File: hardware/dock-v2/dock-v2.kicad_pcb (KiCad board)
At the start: 4 copper layers, 100 x 100 mm, 148 parts, among them J101 TYPE-C-31-M-12, J201 TYPE-C-31-M-12, J202 TYPE-C-31-M-12, J203 TYPE-C-31-M-12, J601 Pogo 7-pin, Q601 2N7002, Q602 2N7002, SW301 SW_Push, SW302 SW_Push, SW401 SW_Push, U101 TPD4E1U06DBVR, U102 CH224A, U103 TPS54331DR, U104 AMS1117-3.3, U201 TPD4E1U06DBVR, U202 SY6280AAC, U203 TPD4E1U06DBVR, U204 TPD4E1U06DBVR, U301 RP2354A, U401 RP2354A, U501 ESP32-C3-MINI-1-H4X, U601 TPD4E1U06DBVR, U602 SY6280AAC, Y301 12MHz, Y401 12MHz

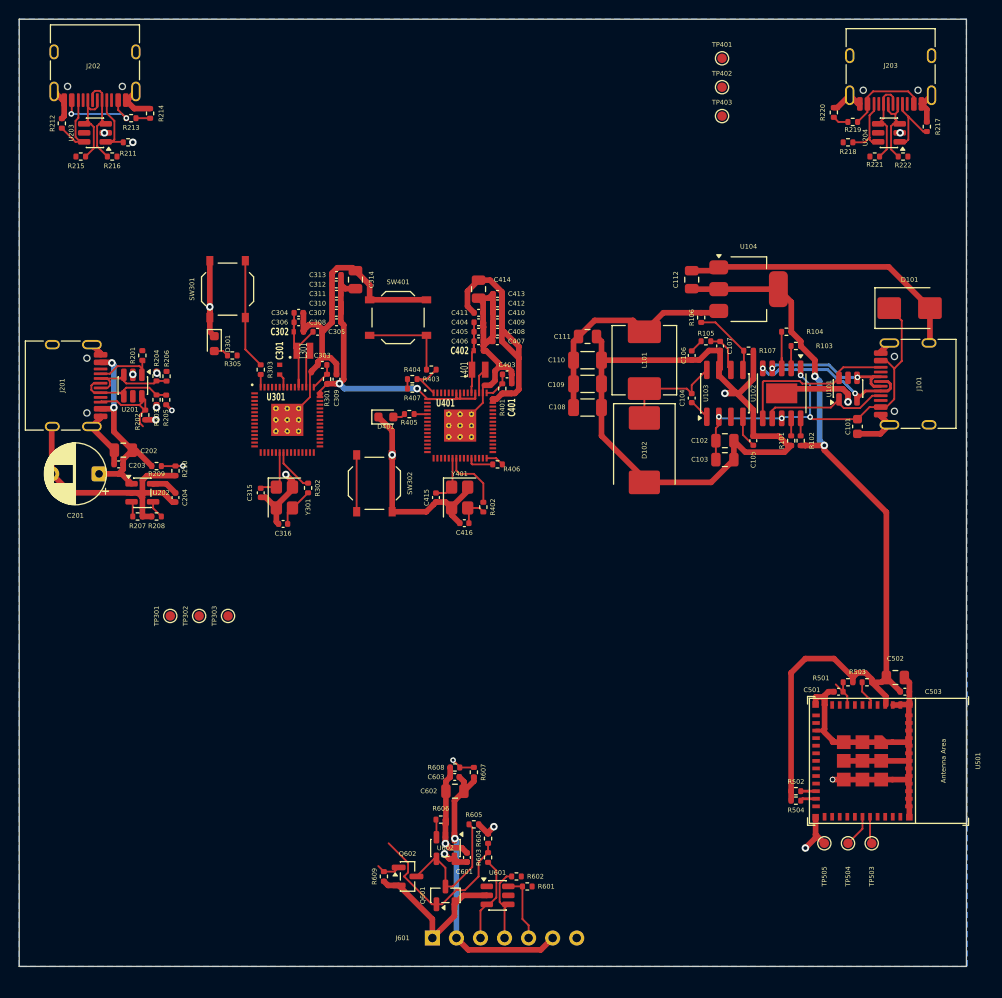
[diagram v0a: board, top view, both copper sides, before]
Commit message: Dock v2: routing complete, SWD test pads removed (user's work, snapshot)
Co-Authored-By: Claude Opus 5.5 <noreply@anthropic.com>
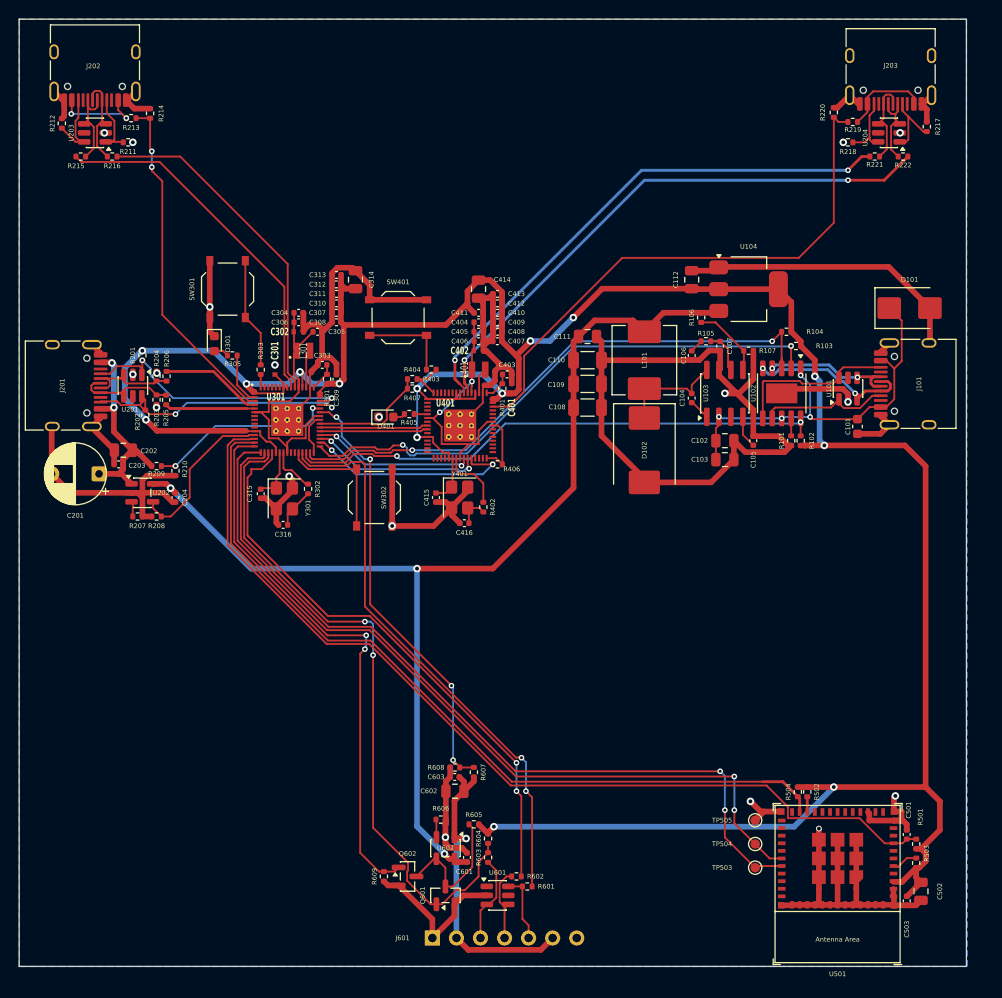
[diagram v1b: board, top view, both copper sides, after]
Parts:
- removed TP301, TP302, TP303, TP401, TP402, TP403: TestPoint, TestPoint:TestPoint_Pad_D1.0mm
- moved C502 22.7 mm to (224.2, 127.1), turned to 90 degrees
- moved C503 22.1 mm to (222.7, 128.1), turned to 90 degrees
- moved R503 19.8 mm to (223.7, 124.1), turned to -90 degrees
- moved R501 18.5 mm to (223.7, 122.1), turned to -90 degrees
- moved C501 16.7 mm to (222.7, 121.1), turned to -90 degrees
- moved U501 14.0 mm to (215.4, 126.3), turned to 180 degrees
- moved TP503 12.6 mm to (206.7, 124.6), turned to -90 degrees
- moved TP504 9.80 mm to (206.7, 122.1), turned to -90 degrees
- moved TP505 7.69 mm to (206.7, 119.6), turned to -90 degrees
- moved SW302 1.50 mm to (166.5, 85.5)
- moved R502 1.20 mm to (212.2, 116.6), turned to -90 degrees
- moved R504 0.95 mm to (211.2, 116.6), turned to -90 degrees
- moved C301 0.50 mm to (156.0, 72.0)
- moved C316 0.10 mm to (156.9, 88.4)
- moved R302 0.10 mm to (159.5, 84.6)
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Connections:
- R305 pad 1: Net-(U301-GPIO2) -> Net-(U301-GPIO0)
- U301 pad 10: KBD_USB_DN -> unconnected-(U301-GPIO7-Pad10)
- U301 pad 12: BLE_TX -> KBD_VBUS_EN
- U301 pad 13: BLE_RX -> BLE_EN
- U301 pad 14: BLE_EN -> BLE_BOOT
- U301 pad 15: BLE_BOOT -> POGO_OFF
- U301 pad 16: POGO_TX -> BLE_TX
- U301 pad 17: POGO_RX -> BLE_RX
- U301 pad 19: POGO_OFF -> POGO_RX
- U301 pad 2: PRS_VBUS_DET -> Net-(U301-GPIO0)
- U301 pad 24: Net-(U301-SWCLK) -> unconnected-(U301-SWCLK-Pad24)
- U301 pad 25: Net-(U301-SWDIO) -> unconnected-(U301-SWDIO-Pad25)
- U301 pad 27: B_LINK_TX -> POGO_TX
- U301 pad 28: B_LINK_RX -> PD_PG
- U301 pad 29: B_RUN -> PD_SDA
- U301 pad 3: unconnected-(U301-GPIO1-Pad3) -> PRS_VBUS_DET
- U301 pad 31: B_BOOTSEL -> PD_SCL
- U301 pad 32: PD_SDA -> B_RUN
- U301 pad 33: PD_SCL -> B_SWDIO
- U301 pad 34: PD_PG -> B_SWCLK
- U301 pad 35: B_SWCLK -> B_LINK_RX
- U301 pad 36: B_SWDIO -> B_LINK_TX
- U301 pad 37: unconnected-(U301-GPIO25-Pad37) -> B_BOOTSEL
- U301 pad 4: Net-(U301-GPIO2) -> KBD_USB_DN
- U301 pad 40: KBD_CC1 -> POGO_5V_SENSE
- U301 pad 41: KBD_CC2 -> KBD_VBUS_SENSE
- U301 pad 42: KBD_VBUS_SENSE -> KBD_CC2
- U301 pad 43: POGO_5V_SENSE -> KBD_CC1
- U301 pad 5: unconnected-(U301-GPIO3-Pad5) -> KBD_USB_DP
- U301 pad 8: KBD_VBUS_EN -> unconnected-(U301-GPIO5-Pad8)
- U301 pad 9: KBD_USB_DP -> unconnected-(U301-GPIO6-Pad9)
- U401 pad 2: B_LINK_RX -> unconnected-(U401-GPIO0-Pad2)
- U401 pad 3: B_LINK_TX -> unconnected-(U401-GPIO1-Pad3)
- U401 pad 4: WRK_VBUS_DET -> unconnected-(U401-GPIO2-Pad4)
- U401 pad 43: unconnected-(U401-GPIO29/ADC3-Pad43) -> WRK_VBUS_DET
- U401 pad 8: unconnected-(U401-GPIO5-Pad8) -> B_LINK_TX
- U401 pad 9: unconnected-(U401-GPIO6-Pad9) -> B_LINK_RX
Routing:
- net 3V3_PWR: track 161.4 -> 324.6 mm, vias 6 -> 14
- net BLE_EN: track 3.69 -> 100.3 mm
- net 5V_PWR: track 30.1 -> 119.5 mm, vias 1 -> 3
- net BLE_BOOT: track 1.70 -> 85.5 mm
- net BLE_RX: track 2.87 -> 86.5 mm, vias 0 -> 2
- net BLE_TX: track 3.43 -> 85.6 mm, vias 0 -> 2
- net POGO_RX: track 0.00 -> 61.0 mm, vias 0 -> 2
- net POGO_TX: track 0.00 -> 60.0 mm, vias 0 -> 2
- net WRK_USB_DN: track 0.00 -> 59.3 mm, vias 0 -> 2
- net WRK_VBUS_DET: track 1.90 -> 59.3 mm
- net WRK_USB_DP: track 0.00 -> 56.8 mm, vias 0 -> 2
- net PD_SCL: track 2.37 -> 58.7 mm, vias 0 -> 2
- net PD_SDA: track 4.96 -> 61.1 mm, vias 0 -> 2
- net POGO_OFF: track 2.58 -> 58.3 mm, vias 0 -> 2
- net PD_PG: track 1.93 -> 57.1 mm, vias 0 -> 2
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
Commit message: Dock v2 PCB: fix unconnected nets, widen power traces, readable silkscreen, 2 copper layers
- MCU A and B IOVDD (pins 30/38) had no 3V3 feed: added an under-chip jumper (A)
  and a top-layer feed to the 3V3 via by the buck (B)
- MCU B's exposed pad sat in a GND pour island: 3V3 bottom ring via moved so the
  plane reaches it; crystal B GND vias added; pour clearance 0.5 -> 0.3 mm
- power traces widened where clearance allows (switch node 1.5 mm, 5 V 1.0 mm,
  VBUS_IN/POGO_5V/KBD_VBUS as far as fits); VBUS_IN vias 0.8/0.4
- silkscreen: refs 0.8/1.0 mm, re-placed clear of pads and parts, labels for
  connectors, buttons, LEDs and ESP32 UART pads; 22 small passives hidden
- copper layers 4 -> 2 (inner layers were empty)
- model/docs: SWD test pads TP301-303/TP401-403 removed

DRC: 0 violations, 0 unconnected, 0 parity issues.

Co-Authored-By: Claude Opus 5.5 <noreply@anthropic.com>
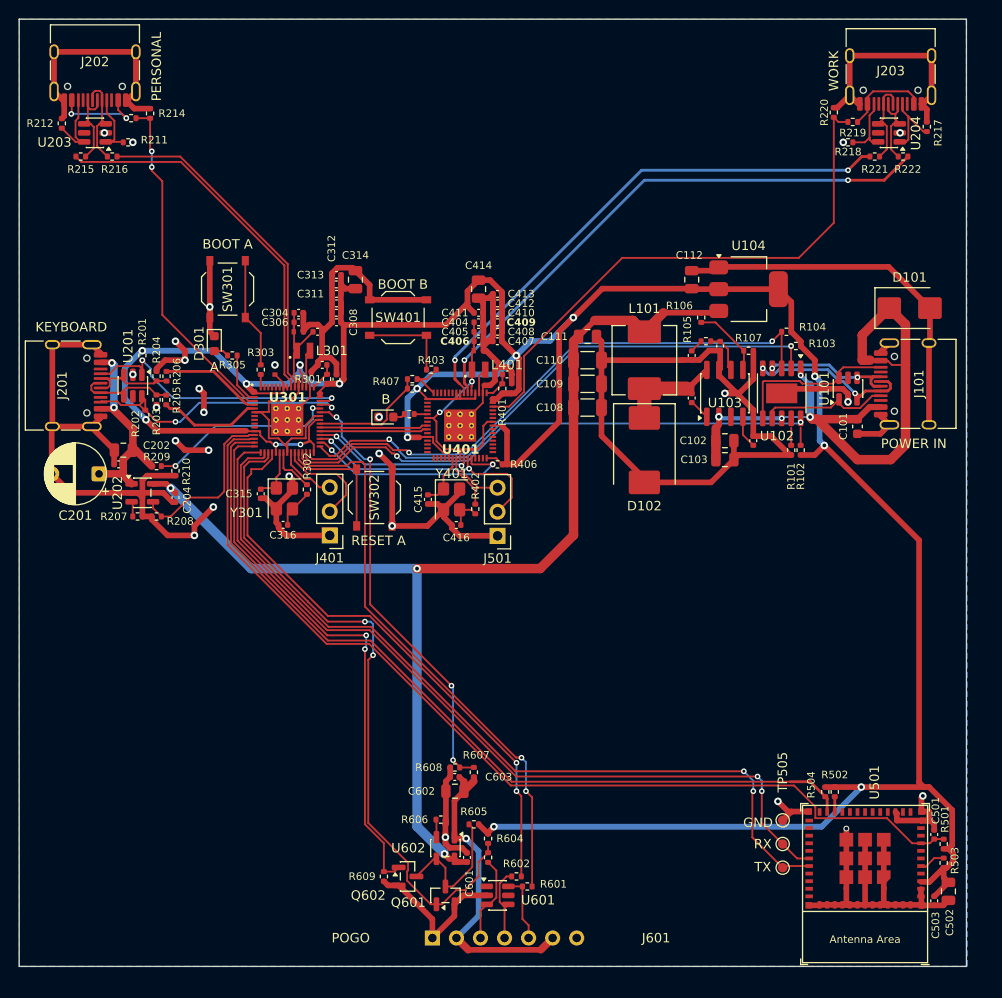
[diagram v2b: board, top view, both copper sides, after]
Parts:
- added J401: Conn_01x03, Connector_PinHeader_2.54mm:PinHeader_1x03_P2.54mm_Vertical, F.Cu at (161.8, 89.5)
- added J501: Conn_01x03, Connector_PinHeader_2.54mm:PinHeader_1x03_P2.54mm_Vertical, F.Cu at (179.5, 89.5)
- moved C501 2.90 mm to (225.6, 121.1)
- moved C502 2.90 mm to (227.1, 127.1)
- moved C503 2.90 mm to (225.6, 128.1)
- moved R501 2.90 mm to (226.6, 122.1)
- moved R502 2.90 mm to (215.1, 116.6)
- moved R503 2.90 mm to (226.6, 124.1)
- moved R504 2.90 mm to (214.1, 116.6)
- moved TP503 2.90 mm to (209.6, 124.6)
- moved TP504 2.90 mm to (209.6, 122.1)
- moved TP505 2.90 mm to (209.6, 119.6)
- moved U501 2.90 mm to (218.3, 126.3)
- moved R101 1.00 mm to (210.5, 80.5)
- moved R102 1.00 mm to (211.5, 80.5)
- moved C415 0.87 mm to (172.2, 85.7)
- moved C416 0.87 mm to (175.1, 88.4)
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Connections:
- R302 pad 1: Net-(C316-Pad2) -> Net-(U301-XOUT)
- R302 pad 2: Net-(U301-XOUT) -> Net-(C316-Pad2)
- U301 pad 24: unconnected-(U301-SWCLK-Pad24) -> Net-(J401-Pin_3)
- U301 pad 25: unconnected-(U301-SWDIO-Pad25) -> Net-(J401-Pin_2)
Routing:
- net GND: track 358.0 -> 452.1 mm, vias 18 -> 26
- net /POWER/VBUS_IN: track 42.1 -> 67.8 mm
- net 3V3_PWR: track 324.6 -> 348.1 mm, vias 14 -> 15
- net Net-(J401-Pin_2): track 0.00 -> 10.9 mm
- net B_SWDIO: track 18.5 -> 27.5 mm
- net Net-(J401-Pin_3): track 0.00 -> 6.36 mm
- net B_SWCLK: track 17.2 -> 22.3 mm
- net 5V_PWR: track 119.5 -> 122.4 mm
- net BLE_EN: track 100.3 -> 103.2 mm
- net BLE_BOOT: track 85.5 -> 88.4 mm
- net BLE_RX: track 86.5 -> 89.2 mm
- net BLE_TX: track 85.6 -> 88.2 mm
- net /MCU_B/B_1V1: track 28.7 -> 30.3 mm
- net KBD_USB_DP: track 9.50 -> 10.9 mm
- net PRS_USB_DP: track 38.6 -> 39.9 mm
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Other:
- copper layers 4 -> 2
- board text added: "A"
- board text added: "B"
- board text added: "BOOT A"
- board text added: "BOOT B"
- board text added: "GND"
- board text added: "KEYBOARD"
- board text added: "PERSONAL"
- board text added: "POGO"
- board text added: "POWER IN"
- board text added: "RESET A"
- board text added: "RX"
- board text added: "TX"
- board text added: "WORK"

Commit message: Dock v2: six M3 mounting holes, U102 CFG1/PG tracks joined, SWD headers in the model
- H1-H6 (MountingHole_3.2mm_M3, unplated) added to the root schematic and placed:
  back (146,39)/(212,39) beside the USB-C ports, sides (133,58)/(225,58),
  front (160,131)/(200,131) either side of the pogo; symmetric about x = 179-180,
  clear of the ESP32 antenna
- R101/R102 tracks ended 1 mm short of U102 pins 9/10: joined
- J401 (SWD A) and J501 (SWD B) added to the connection model and docs

DRC: 0 violations, 0 unconnected, 0 parity issues. ERC: 1 old warning.

Co-Authored-By: Claude Opus 5.5 <noreply@anthropic.com>
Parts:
- added H1: M3, MountingHole:MountingHole_3.2mm_M3, F.Cu at (146.0, 39.0)
- added H2: M3, MountingHole:MountingHole_3.2mm_M3, F.Cu at (212.0, 39.0)
- added H3: M3, MountingHole:MountingHole_3.2mm_M3, F.Cu at (133.0, 58.0)
- added H4: M3, MountingHole:MountingHole_3.2mm_M3, F.Cu at (225.0, 58.0)
- added H5: M3, MountingHole:MountingHole_3.2mm_M3, F.Cu at (160.0, 131.0)
- added H6: M3, MountingHole:MountingHole_3.2mm_M3, F.Cu at (200.0, 131.0)
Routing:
- net Net-(U102-CFG1): track 1.85 -> 2.85 mm
- net PD_PG: track 57.8 -> 58.4 mm

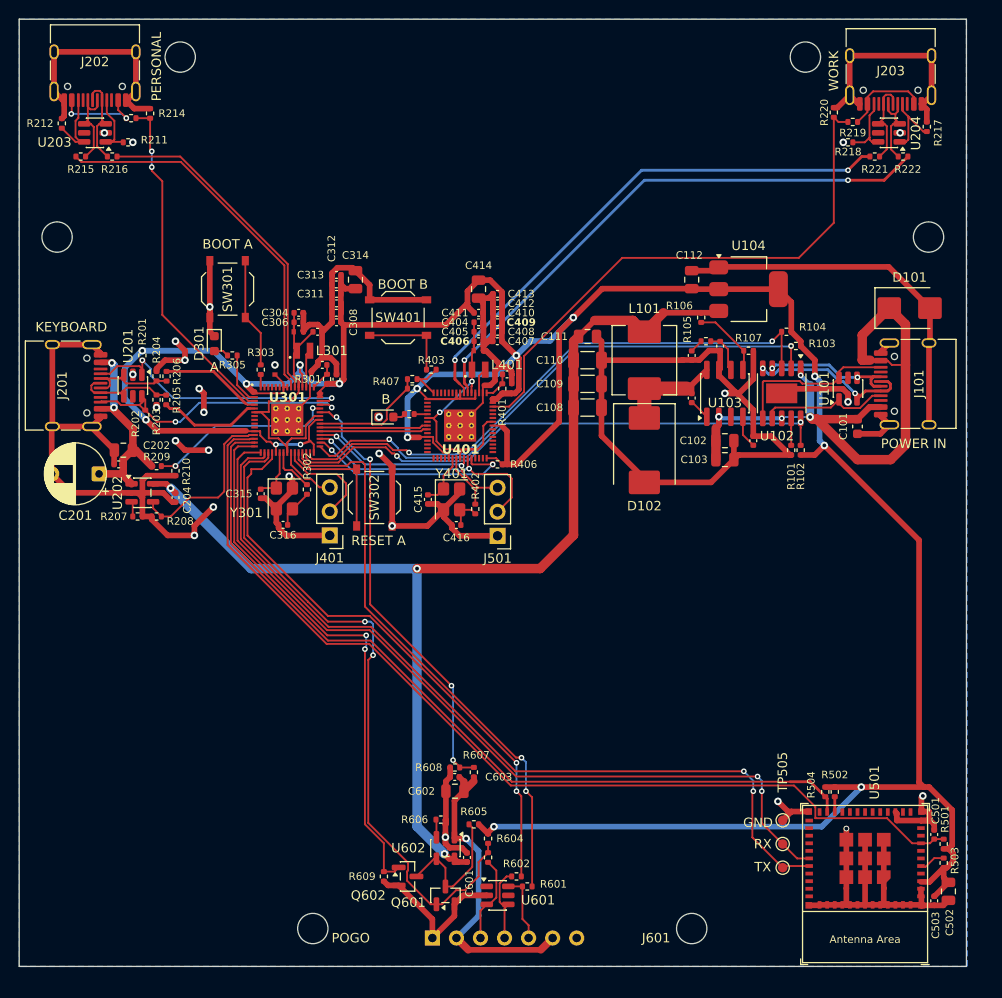
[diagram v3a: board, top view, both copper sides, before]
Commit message: Dock v2: extra mounting holes around the USB-C ports (user's work), H7-H10 given own symbols
The four added holes were copies of H5 (same reference and schematic link);
renamed H7-H10 with their own MountingHole symbols on the root sheet.
DRC: 0 violations, 0 unconnected, 0 parity issues.

Co-Authored-By: Claude Opus 5.5 <noreply@anthropic.com>
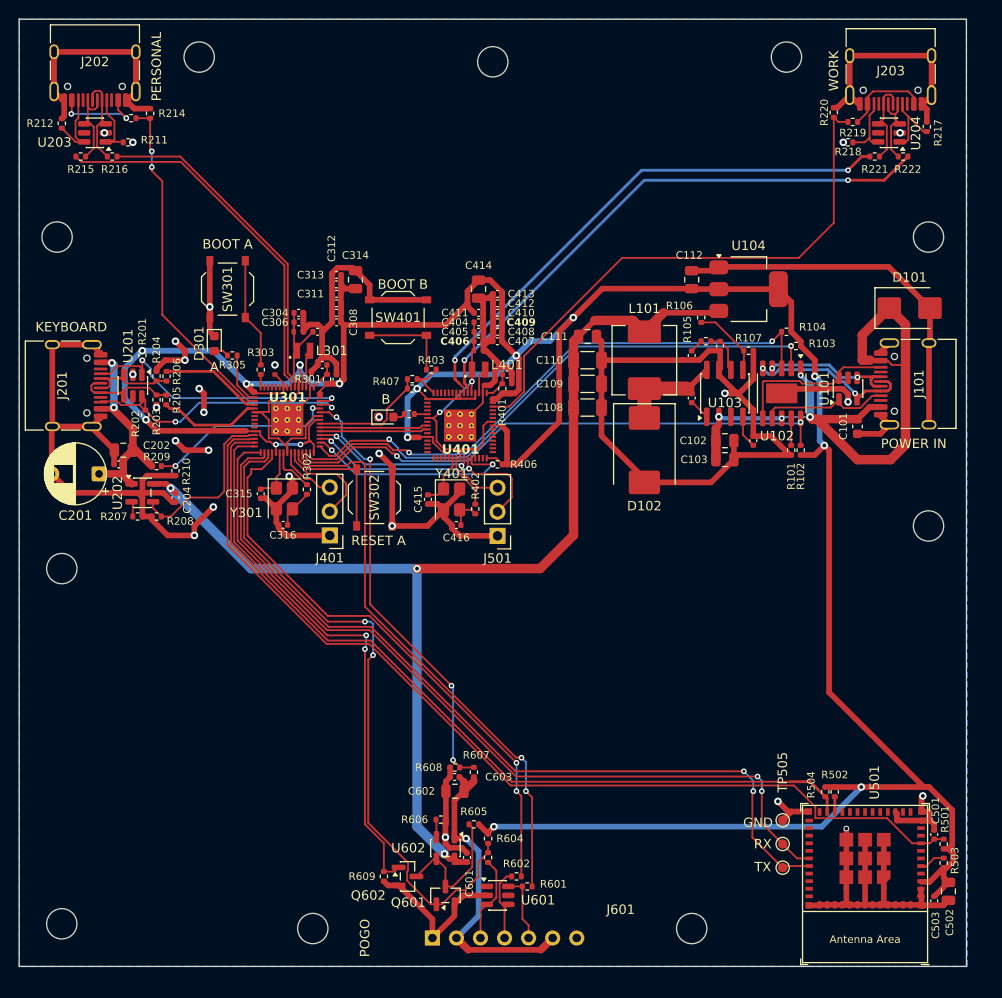
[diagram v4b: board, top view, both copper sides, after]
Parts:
- added H10: M3, MountingHole:MountingHole_3.2mm_M3, F.Cu at (225.0, 88.5)
- added H7: M3, MountingHole:MountingHole_3.2mm_M3, F.Cu at (133.5, 130.5)
- added H8: M3, MountingHole:MountingHole_3.2mm_M3, F.Cu at (133.5, 93.0)
- added H9: M3, MountingHole:MountingHole_3.2mm_M3, F.Cu at (179.0, 39.5)
- moved H1 2.00 mm to (148.0, 39.0)
- moved H2 2.00 mm to (210.0, 39.0)

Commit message: Dock v2: J601 becomes a JST-XH 7-pin cable header (pad docks on top)
- pad sits on top of the dock (decided): straight Motorobit 7-pin pogo contacts
  on a small lid board (same design as the pad's pogo board), cabled 1:1 to J601
- J601: B7B-XH-A (LCSC C144398) on the original pin row; 5 V link between
  pins 2/6 moved 0.75 mm lower to clear the larger XH pads; silk trimmed at the edge
- pad MCU decided: ESP32-S3-MINI-1-N8 (README)
- docs: pogo, placement, DESIGN §15/§17, README, generated guides

DRC: 0 violations, 0 unconnected, 0 parity issues.

Co-Authored-By: Claude Opus 5.5 <noreply@anthropic.com>
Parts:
- J601: value Pogo 7-pin -> B7B-XH-A (to lid pogo board); footprint dock:Pogo-7 -> Connector_JST:JST_XH_B7B-XH-A_1x07_P2.50mm_Vertical
- moved J601 7.50 mm to (172.7, 132.0)
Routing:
- net POGO_5V: track 33.5 -> 36.2 mm

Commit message: Dock v2: J601 uses a project copy of the XH footprint with the silk trimmed at the edge (no library-mismatch warning)
Co-Authored-By: Claude Opus 5.5 <noreply@anthropic.com>
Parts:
- J601: footprint Connector_JST:JST_XH_B7B-XH-A_1x07_P2.50mm_Vertical -> dock:JST_XH_B7B-XH-A_1x07_P2.50mm_Vertical_EdgeTrim
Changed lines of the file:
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@@
 		)
 	)
-	(footprint "Connector_JST:JST_XH_B7B-XH-A_1x07_P2.50mm_Vertical"
+	(footprint "dock:JST_XH_B7B-XH-A_1x07_P2.50mm_Vertical_EdgeTrim"
 		(layer "F.Cu")
 		(at 172.74 132)
